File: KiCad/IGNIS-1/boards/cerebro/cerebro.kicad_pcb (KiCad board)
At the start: 2 copper layers, 62 x 62 mm, 17 parts, among them J40 Backplane_2x10, Q1 MMBT3904, U10 ESP32-WROOM-32E DevKit 40p

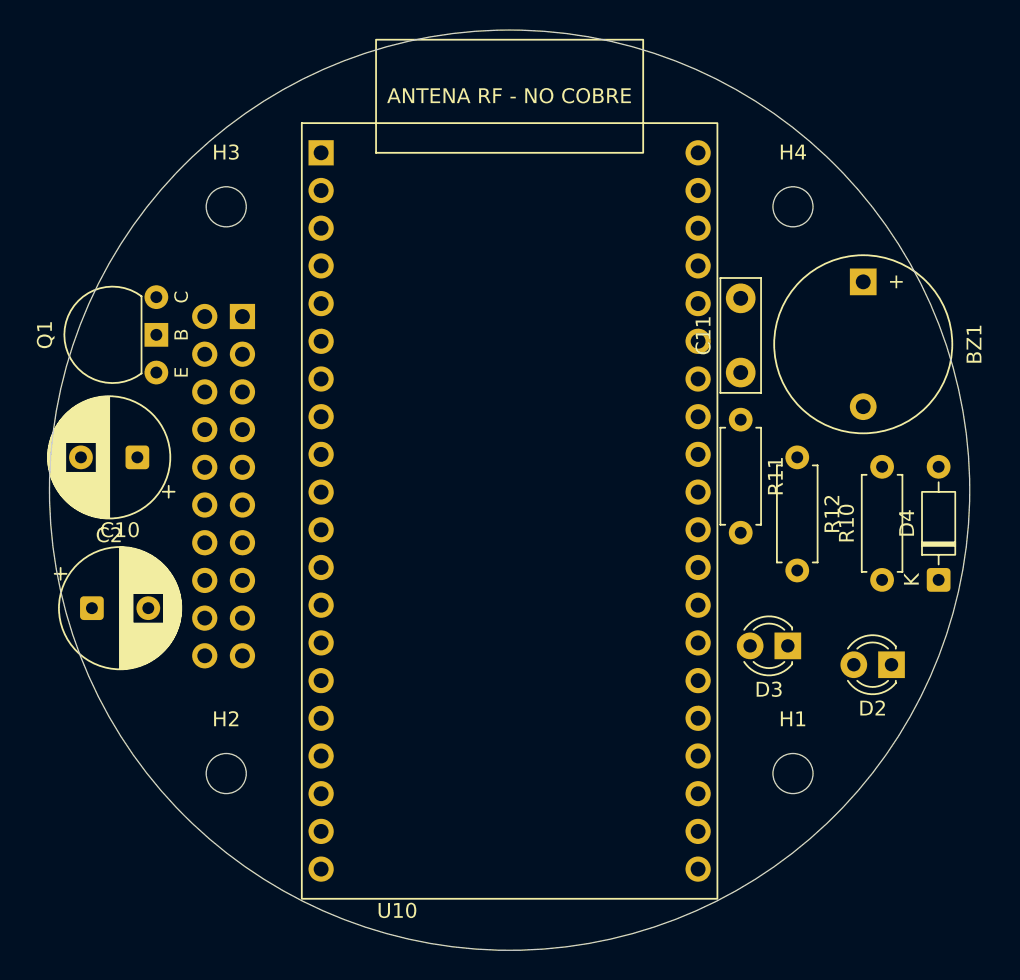
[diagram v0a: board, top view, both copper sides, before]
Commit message: 5 boards separados, falta ajustar dimensiones de BME280 y MQ-135
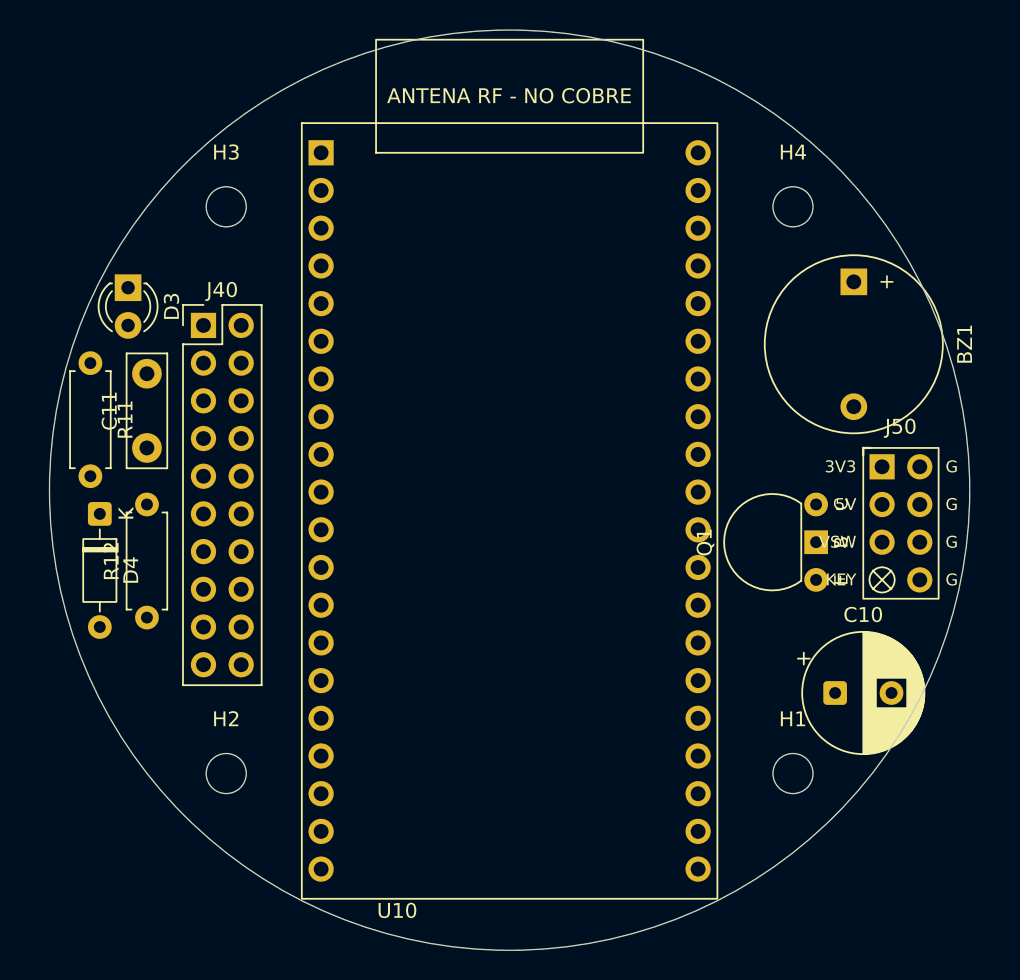
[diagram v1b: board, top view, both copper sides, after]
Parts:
- removed C2: 100uF, Capacitor_THT:CP_Radial_D8.0mm_P3.80mm
- removed D2: PWR_grn, LED_THT:LED_D3.0mm
- removed R10: 1k, Resistor_THT:R_Axial_DIN0207_L6.3mm_D2.5mm_P7.62mm_Horizontal
- added J50: J_PWR_2x4, IGNIS1:J_PWR_2x4_Keyed, F.Cu at (126.4, 102.2)
- J40: moved to F.Cu
- moved D4 56.7 mm to (72.4, 101.6), turned to -90 degrees
- moved D3 50.6 mm to (74.3, 86.4), turned to -90 degrees
- moved C10 50.4 mm to (121.9, 113.7)
- moved Q1 46.6 mm to (120.7, 103.5)
- moved R12 45.1 mm to (75.6, 108.6), turned to 90 degrees
- moved R11 44.0 mm to (71.8, 91.4)
- moved C11 40.3 mm to (75.6, 97.2)
- moved J40 2.69 mm to (79.4, 88.9), turned to 0 degrees
- moved BZ1 0.64 mm to (123.2, 90.2)
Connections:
- J40 pad 1: +3V3 -> unconnected-(J40-Pin_1-Pad1)

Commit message: Se agregaron tracks. PCB Cerebro libre de errores.
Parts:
- moved C10 1.42 mm to (121.3, 112.4)
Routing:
- net GND: track 0.00 -> 158.2 mm, vias 0 -> 4
- net +3V3: track 0.00 -> 131.4 mm
- net /BUZZ_C: track 0.00 -> 94.2 mm, vias 0 -> 2
- net Net-(Q1-B): track 0.00 -> 81.6 mm, vias 0 -> 2
- net GPS_RX: track 0.00 -> 75.3 mm, vias 0 -> 3
- net SCK: track 0.00 -> 72.4 mm, vias 0 -> 3
- net /STATUS: track 0.00 -> 63.8 mm, vias 0 -> 2
- net MISO: track 0.00 -> 58.6 mm, vias 0 -> 2
- net MOSI: track 0.00 -> 55.7 mm, vias 0 -> 1
- net /BUZZER: track 0.00 -> 42.3 mm, vias 0 -> 1
- net GPS_TX: track 0.00 -> 37.6 mm, vias 0 -> 2
- net NSS_LORA: track 0.00 -> 35.9 mm, vias 0 -> 2
- net DIO0: track 0.00 -> 25.0 mm, vias 0 -> 1
- net MPU_INT: track 0.00 -> 21.8 mm, vias 0 -> 2
- net MQ_AOUT: track 0.00 -> 15.8 mm, vias 0 -> 1
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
